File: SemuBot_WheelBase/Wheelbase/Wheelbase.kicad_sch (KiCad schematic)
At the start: 47 parts, among them J1 10155435-00011LF, J10 B5B-XH-A_LF__SN_, J11 B5B-XH-A_LF__SN_, J12 B5B-XH-A_LF__SN_, J13 MTSW-104-09-L-S-400, J14 XT30PW-M, J15 MTSW-104-09-L-S-400, J2 MTSW-102-09-L-S-400, J3 MR30PW-M, J4 B5B-XH-A_LF__SN_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

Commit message: Encoder fix
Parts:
- added C2: 100nF, Capacitor_SMD:C_0603_1608Metric_Pad1.08x0.95mm_HandSolder, symbol Device:C
- added D1: green, LED_SMD:LED_0603_1608Metric_Pad1.05x0.95mm_HandSolder, symbol Device:LED
- added R23: 10k, Resistor_SMD:R_0603_1608Metric_Pad0.98x0.95mm_HandSolder, symbol Device:R
- added R24: 100, Resistor_SMD:R_0603_1608Metric_Pad0.98x0.95mm_HandSolder, symbol Device:R
- added R25, R26: 3.3K, Resistor_SMD:R_0603_1608Metric_Pad0.98x0.95mm_HandSolder, symbol Device:R
- added S1: SWT0211-050010GSA_REVA, switch:SW_SWT0211-050010GSA_REVA, symbol SWT0211-050010GSA_REVA:SWT0211-050010GSA_REVA
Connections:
- net +3.3V: now also R23.1, R26.2
- net GND: now also C2.1, R25.2, S1.3, S1.4
- net MOTOR1_DIR: now also U1.11 (PC3); no longer U1.37 (PC6)
- net MOTOR2_DIR: now also U1.25 (PC5); no longer U1.21 (PA5)
- net MOTOR2_PWM: now also U1.37 (PC6); no longer U1.22 (PA6)
- net Motor_1/HAL_1: now also J4.2; no longer J4.4
- net Motor_1/HAL_3: now also J4.4; no longer J4.2
- net NRST: now also C2.2, R23.2, R24.1
- net motor3_nBRAKE: now also U1.26 (PB0); no longer U1.23 (PA7)
- net at U1.3 (PC14): now also D1.2 (A)
- net enc_2_data: now reaches U1.4 (PC15)
- net enc_2_data: now also J11.2
- net enc_3_data: now reaches U1.57 (PB5)
- net enc_3_data: now also J12.2
- net SSI_DATA renamed enc_1_data
- net enc_1_data: no longer J11.2, J12.2
- new net: D1.1 (K), R25.1
- new net: R24.2, S1.1, S1.2
- new net SPI1_MISO: R26.1, U1.22 (PA6)
- new net SPI1_MOSI: U1.23 (PA7)
- new net SPI1_SCK: U1.21 (PA5)
- no-connect marks 16 -> 10
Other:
- sheet Motor_1 ports: added SPI1_MISO, SPI1_MOSI, SPI1_SCLK; removed none
- sheet Motor_2 ports: added SPI1_MISO, SPI1_MOSI, SPI1_SCLK; removed none
- sheet Motor_3 ports: added SPI1_MISO, SPI1_MOSI, SPI1_SCLK; removed none
- moved on the sheet: D2, R6

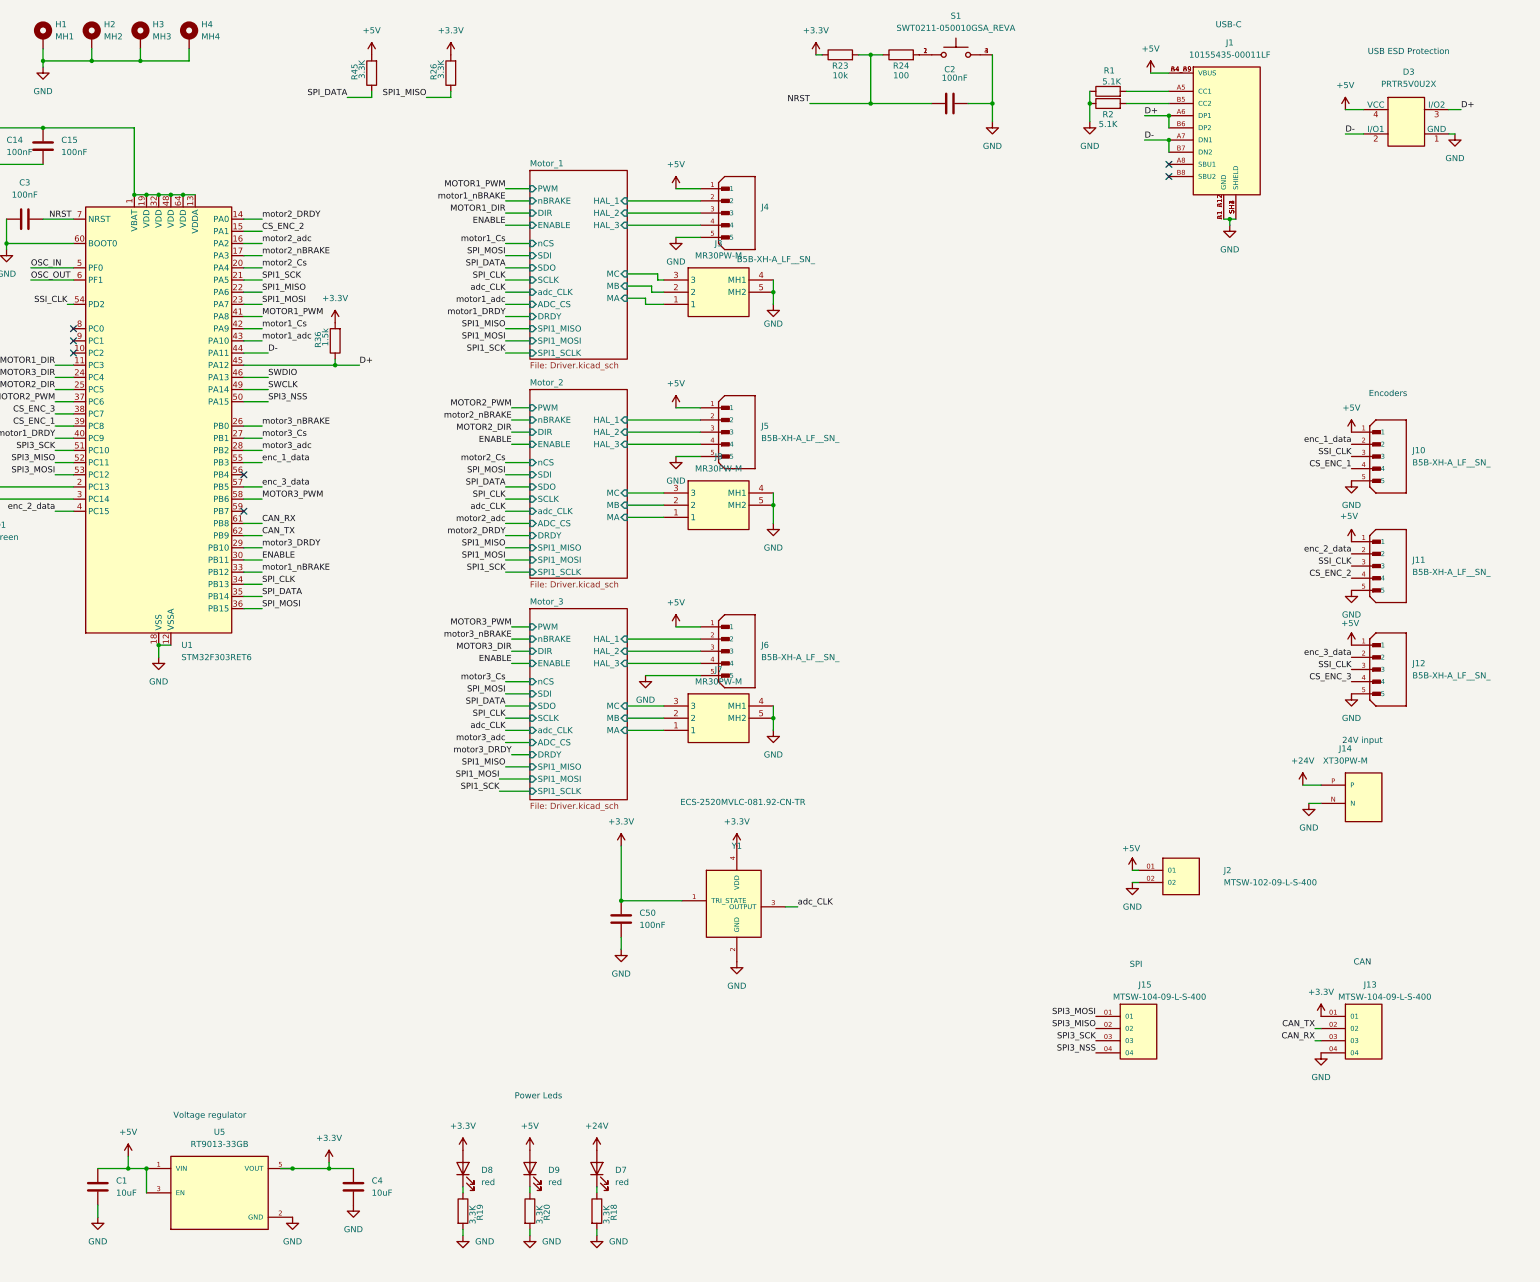
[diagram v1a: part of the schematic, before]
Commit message: Updated mosfet symbols and organization
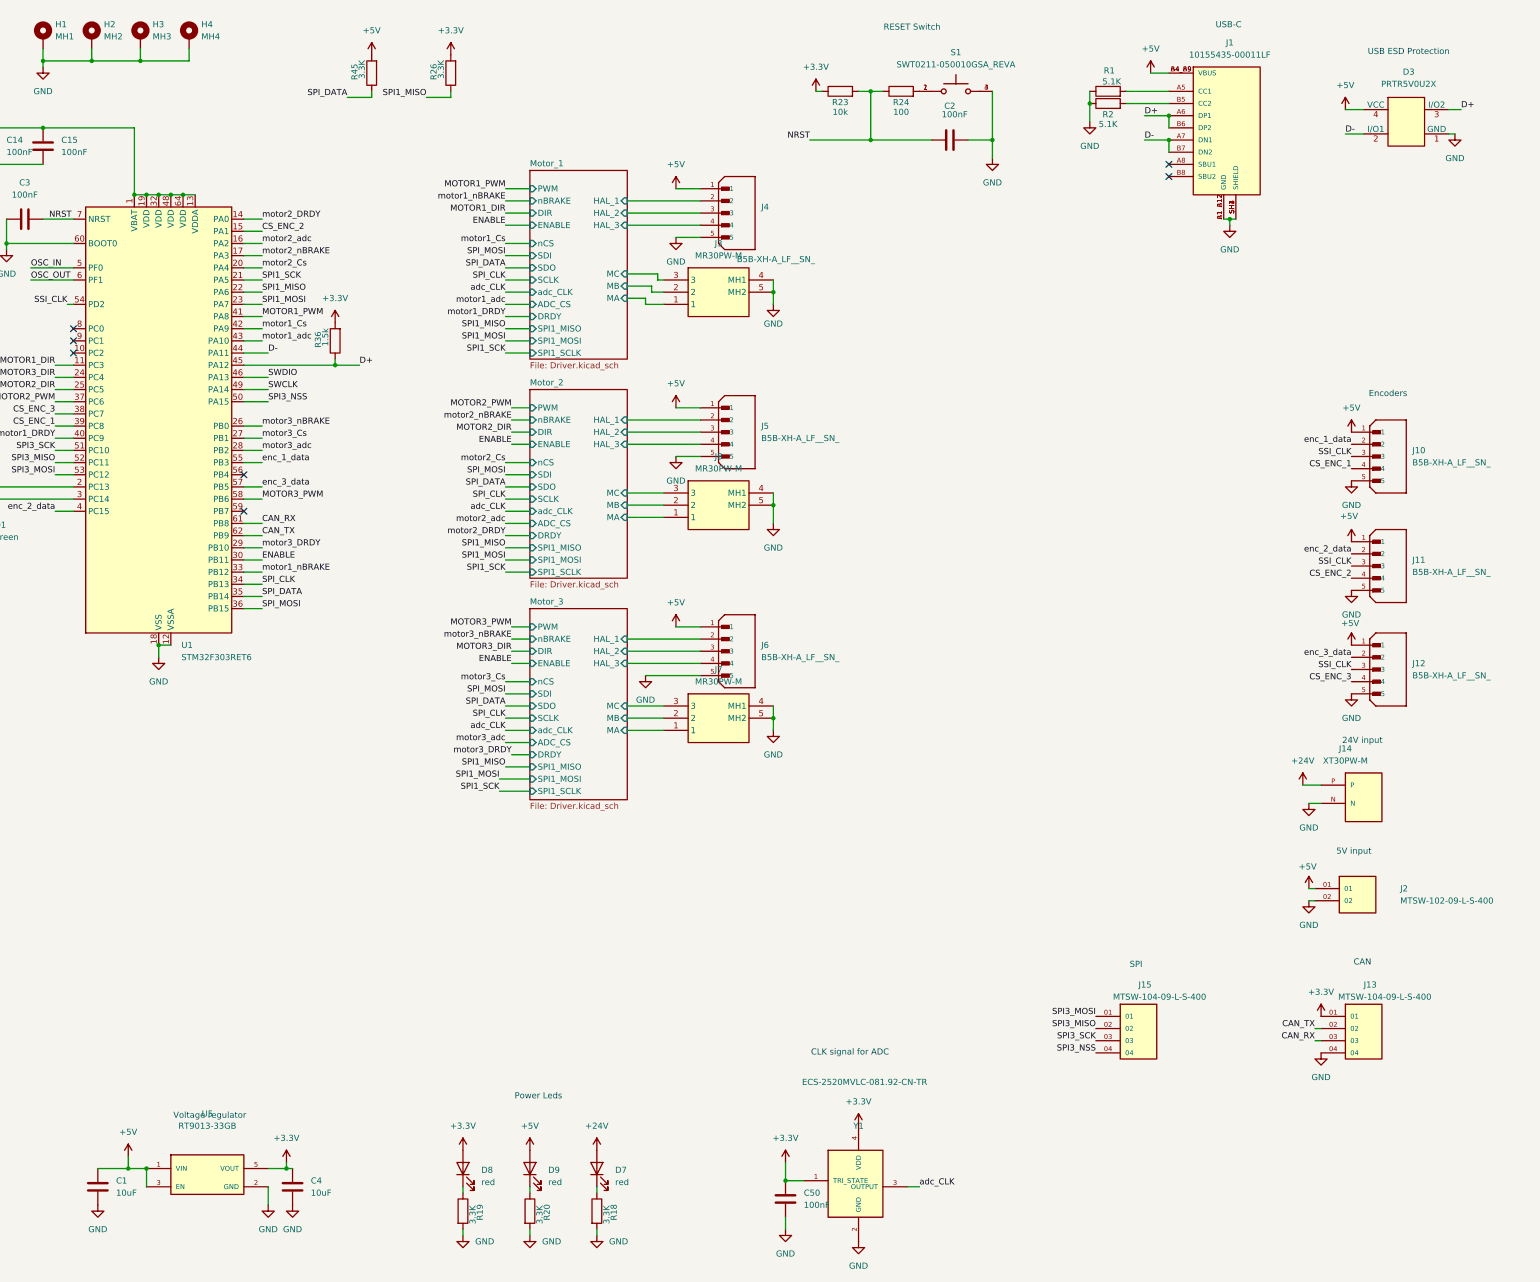
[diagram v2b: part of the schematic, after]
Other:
- note added: "5V input"
- note added: "CLK signal for ADC"
- note added: "RESET Switch"
- moved on the sheet: C2, C4, C50, J2, R23, R24, S1, U5, Y1
